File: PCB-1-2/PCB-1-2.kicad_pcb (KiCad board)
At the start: 2 copper layers, 4 parts, among them U1 LTC1298IS8_PBF, U2 LTC1451IS8-PBF, U3 HI-3110PSIF, U4 FT231XS-R

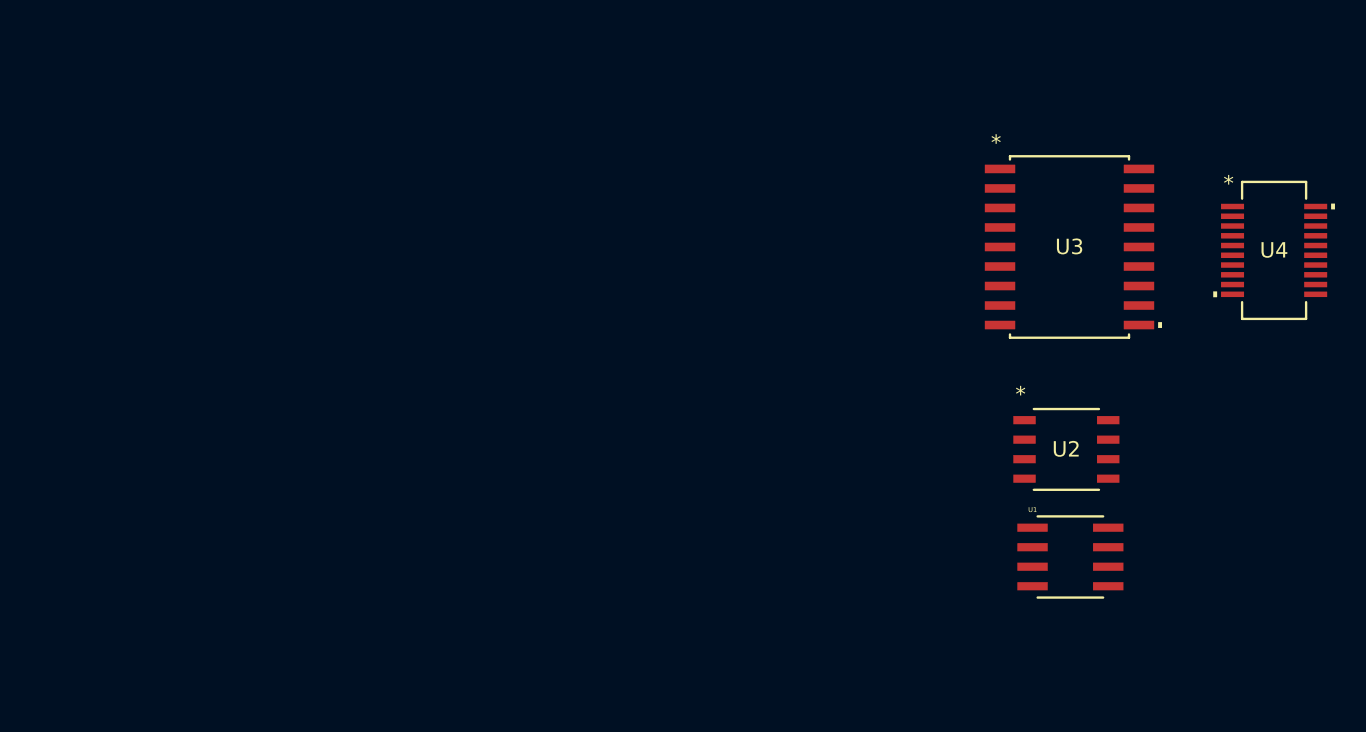
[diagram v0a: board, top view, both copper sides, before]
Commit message: Added misc components and added complimentary parts for the MCU
- Added the ADP7104 5v & 3.3V LDO's
- Added the Watchdog and connected it
- Added complimentary components for STM32
- Figured out the desired crystal and complimentary components
- Added Debug port for the ST-Link v3-MINIE
- Assigned footprints for all capacitors and most resistors
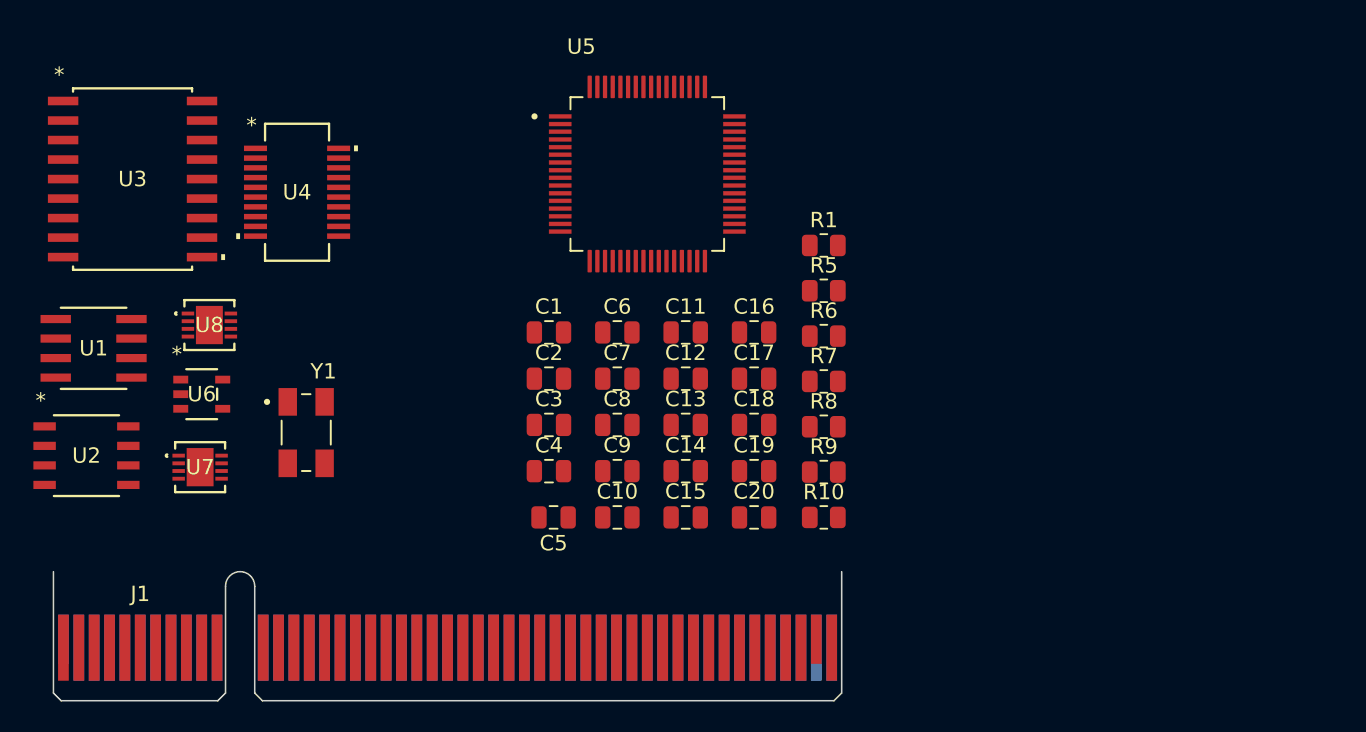
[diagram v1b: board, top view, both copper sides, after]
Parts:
- added C1: 4.7uF, Capacitor_SMD:C_0805_2012Metric, F.Cu at (61.6, 43.0)
- added C10: 100nF, Capacitor_SMD:C_0805_2012Metric, F.Cu at (66.0, 55.0)
- added C11: 100nF, Capacitor_SMD:C_0805_2012Metric, F.Cu at (70.5, 43.0)
- added C12: 10uF, Capacitor_SMD:C_0805_2012Metric, F.Cu at (70.5, 46.0)
- added C13: 10nF, Capacitor_SMD:C_0805_2012Metric, F.Cu at (70.5, 49.0)
- added C14: 1uF, Capacitor_SMD:C_0805_2012Metric, F.Cu at (70.5, 52.0)
- added C15: 1uF, Capacitor_SMD:C_0805_2012Metric, F.Cu at (70.5, 55.0)
- added C16: 10pF, Capacitor_SMD:C_0805_2012Metric, F.Cu at (75.0, 43.0)
- added C17: 10pF, Capacitor_SMD:C_0805_2012Metric, F.Cu at (75.0, 46.0)
- added C18: 2.2uF, Capacitor_SMD:C_0805_2012Metric, F.Cu at (75.0, 49.0)
- added C19: 2.2uF, Capacitor_SMD:C_0805_2012Metric, F.Cu at (75.0, 52.0)
- added C2: .1uF, Capacitor_SMD:C_0805_2012Metric, F.Cu at (61.6, 46.0)
- added C20: .1uF, Capacitor_SMD:C_0805_2012Metric, F.Cu at (75.0, 55.0)
- added C3: 47pF, Capacitor_SMD:C_0805_2012Metric, F.Cu at (61.6, 49.0)
- added C4: 47pF, Capacitor_SMD:C_0805_2012Metric, F.Cu at (61.6, 52.0)
- added C5: 100nF, Capacitor_SMD:C_0805_2012Metric, F.Cu at (61.9, 55.0)
- added C6: 10nF, Capacitor_SMD:C_0805_2012Metric, F.Cu at (66.0, 43.0)
- added C7: 100nF, Capacitor_SMD:C_0805_2012Metric, F.Cu at (66.0, 46.0)
- added C8: 100nF, Capacitor_SMD:C_0805_2012Metric, F.Cu at (66.0, 49.0)
- added C9: 100nF, Capacitor_SMD:C_0805_2012Metric, F.Cu at (66.0, 52.0)
- added J1: Bus_PCI_Express_x8, Connector_PCBEdge:BUS_PCIexpress_x8, F.Cu at (30.0, 63.5)
- added R1: 5.1K, Resistor_SMD:R_0805_2012Metric, F.Cu at (79.5, 37.3)
- added R10: 100k, Resistor_SMD:R_0805_2012Metric, F.Cu at (79.5, 55.0)
- added R5: 100k, Resistor_SMD:R_0805_2012Metric, F.Cu at (79.5, 40.3)
- added R6: 17.4k, Resistor_SMD:R_0805_2012Metric, F.Cu at (79.5, 43.2)
- added R7: 5.6k, Resistor_SMD:R_0805_2012Metric, F.Cu at (79.5, 46.2)
- added R8: 17.4k, Resistor_SMD:R_0805_2012Metric, F.Cu at (79.5, 49.1)
- added R9: 10k, Resistor_SMD:R_0805_2012Metric, F.Cu at (79.5, 52.1)
- added U5: STM32F103RBT6, SDII LIB:QFP50P1200X1200X160-64N, F.Cu at (68.0, 32.7)
- added U6: STWD100YNXWY3F, SDII LIB:SOT23-5_STM, F.Cu at (39.0, 47.0)
- added U7: ADP7104ACPZ-5V, SDII LIB:CP_8_5_ADI, F.Cu at (38.9, 51.8)
- added U8: ADP7104ACPZ-3.3V, SDII LIB:CP_8_5_ADI, F.Cu at (39.5, 42.5)
- added Y1: 8MHz Crystal, SDII LIB:XTAL_ABM3B-8.000MHZ-10-1-U-T, F.Cu at (45.8, 49.5)
- moved U1 65.0 mm to (32.0, 44.0)
- moved U2 63.8 mm to (31.5, 51.0)
- moved U4 63.7 mm to (45.2, 33.9)
- moved U3 61.1 mm to (34.5, 33.0)
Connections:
- U1 pad 1: unconnected-(U1-*CS/SHDN-Pad1) -> SPI2_CS
- U1 pad 2: unconnected-(U1-CH0-Pad2) -> ADC_CH0
- U1 pad 3: unconnected-(U1-CH1-Pad3) -> ADC_CH1
- U1 pad 4: unconnected-(U1-GND-Pad4) -> +5V
- U1 pad 5: unconnected-(U1-DIN-Pad5) -> SPI2_MOSI
- U1 pad 6: unconnected-(U1-DOUT-Pad6) -> SPI2_MISO
- U1 pad 7: unconnected-(U1-CLK-Pad7) -> SPI2_CLK
- U1 pad 8: unconnected-(U1-VCC(VREF)-Pad8) -> +5V
- U2 pad 1: unconnected-(U2-CLK-Pad1) -> SPI2_CLK
- U2 pad 2: unconnected-(U2-DIN-Pad2) -> SPI2_MOSI
- U2 pad 3: unconnected-(U2-*CS/LD-Pad3) -> SPI2_CS
- U2 pad 4: unconnected-(U2-DOUT-Pad4) -> SPI2_MISO
- U2 pad 5: unconnected-(U2-GND-Pad5) -> +5V
- U2 pad 6: unconnected-(U2-REF-Pad6) -> Net-(U2-REF)
- U2 pad 7: unconnected-(U2-VOUT-Pad7) -> DAC_OUT
- U2 pad 8: unconnected-(U2-VCC-Pad8) -> Net-(U2-REF)
- U4 pad 11: unconnected-(U4-USBDP-Pad11) -> Net-(U4-USBDP)
- U4 pad 12: unconnected-(U4-USBDM-Pad12) -> Net-(U4-USBDM)
- U4 pad 13: unconnected-(U4-3V3OUT-Pad13) -> FT231_3V3OUT
- U4 pad 14: unconnected-(U4-RESET#-Pad14) -> FT231_3V3OUT
- U4 pad 15: unconnected-(U4-VCC-Pad15) -> Net-(U4-VCC)
- U4 pad 16: unconnected-(U4-GND-Pad16) -> Net-(C5-Pad2)
- U4 pad 3: unconnected-(U4-VCCIO-Pad3) -> FT231_3V3OUT
- U4 pad 6: unconnected-(U4-GND-Pad6) -> Net-(C5-Pad2)
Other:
- board outline added: 51.3 x 8.4 mm

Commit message: Updated a few things
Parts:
- moved U4 26.7 mm to (71.3, 28.2)
- moved U8 18.0 mm to (52.5, 55.0)
- moved U5 11.2 mm to (57.2, 35.7)
- moved Y1 9.67 mm to (44.0, 40.0)
- moved U7 8.73 mm to (47.0, 55.0)
- moved C5 7.50 mm to (69.4, 55.0)
- moved C10 7.50 mm to (73.5, 55.0)
- moved C11 7.50 mm to (78.0, 43.0)
- moved C12 7.50 mm to (78.0, 46.0)
- moved C13 7.50 mm to (78.0, 49.0)
- moved C14 7.50 mm to (78.0, 52.0)
- moved C15 7.50 mm to (78.0, 55.0)
- moved C16 7.50 mm to (82.5, 43.0)
- moved C17 7.50 mm to (82.5, 46.0)
- moved C18 7.50 mm to (82.5, 49.0)
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
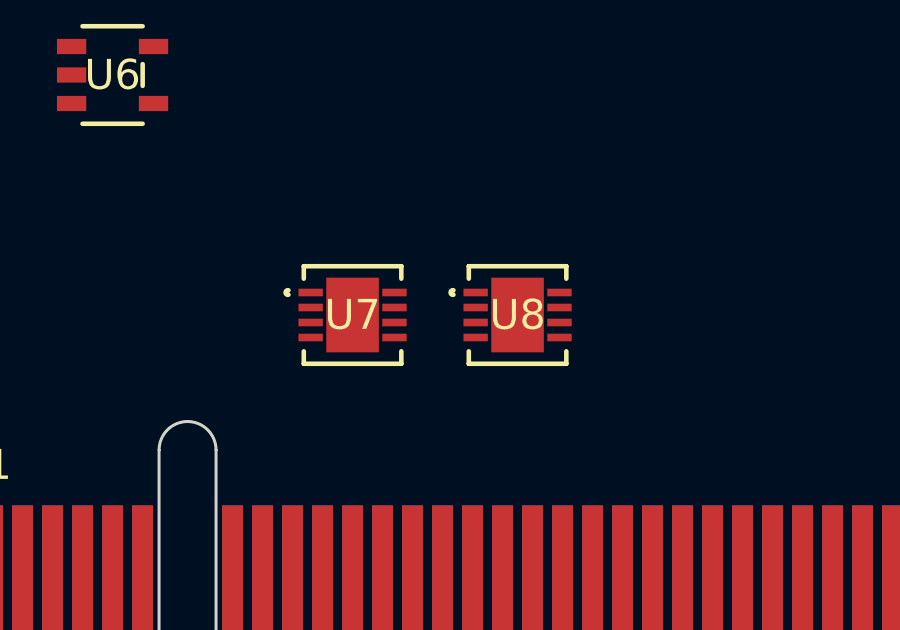
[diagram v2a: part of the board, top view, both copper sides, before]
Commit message: Finished adding connections to the FTDI chip
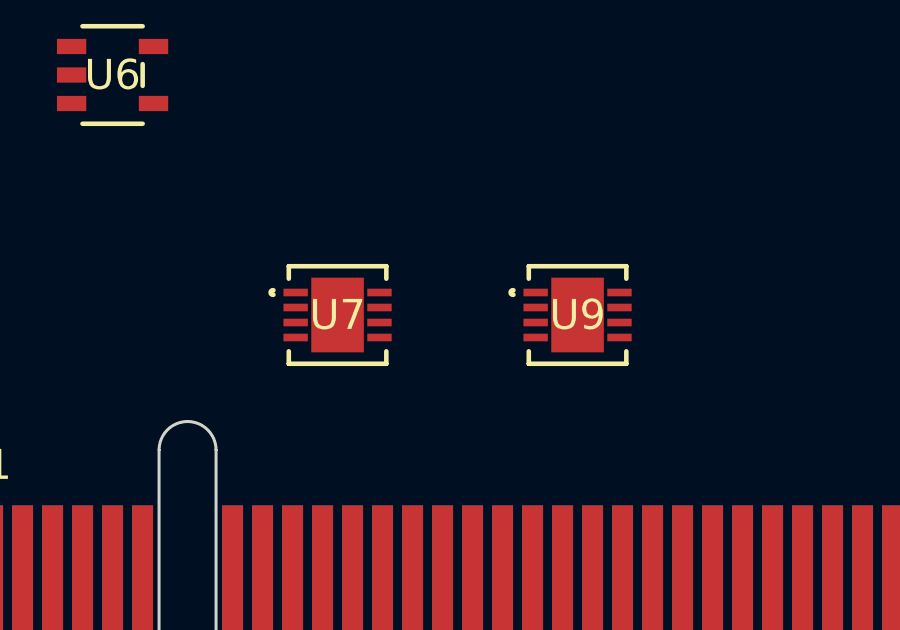
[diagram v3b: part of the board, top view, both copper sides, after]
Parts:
- removed U8: ADP7104ACPZ-3.3V, SDII LIB:CP_8_5_ADI
- added U9: ADP7104ACPZ-R7 (5v), SDII LIB:CP_8_5_ADI, F.Cu at (54.5, 55.0)
- C12: value 10uF -> 4.7uF
- U7: value ADP7104ACPZ-5V -> ADP7104ACPZ-R7 (v3.3)
- moved U7 0.50 mm to (46.5, 55.0)
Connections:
- net Net-(U5-PD0_OSC_IN) renamed /OSC_IN
- net Net-(U5-PD1_OSC_OUT) renamed /OSC_OUT
- C1 pad 1: +5V -> V+_FROM_PCIE
- C1 pad 2: +5V -> V+_FROM_PCIE
- C10 pad 1: +5V -> V+_FROM_PCIE
- C11 pad 1: +5V -> V+_FROM_PCIE
- C12 pad 1: +5V -> V+_FROM_PCIE
- C13 pad 1: +3.3VA -> +3.3V
- C13 pad 2: +5V -> V+_FROM_PCIE
- C14 pad 1: +3.3VA -> +3.3V
- C14 pad 2: +5V -> V+_FROM_PCIE
- C15 pad 1: +3.3VA -> +3.3V
- C15 pad 2: +5V -> V+_FROM_PCIE
- C16 pad 2: +5V -> V+_FROM_PCIE
- C17 pad 2: +5V -> V+_FROM_PCIE
- C18 pad 1: +5V -> V+_FROM_PCIE
- C18 pad 2: +5V -> V+_FROM_PCIE
- C19 pad 2: +5V -> V+_FROM_PCIE
- C2 pad 2: +5V -> V+_FROM_PCIE
- C20 pad 2: +5V -> V+_FROM_PCIE
- C3 pad 2: +5V -> V+_FROM_PCIE
- C4 pad 2: +5V -> V+_FROM_PCIE
- C7 pad 1: +5V -> V+_FROM_PCIE
- C8 pad 1: +5V -> V+_FROM_PCIE
- C9 pad 1: +5V -> V+_FROM_PCIE
- R1 pad 2: +5V -> V+_FROM_PCIE
- R10 pad 2: Net-(U8-PG) -> Net-(U7-PG)
- R5 pad 1: +5V -> V+_FROM_PCIE
- R5 pad 2: Net-(U7-PG) -> Net-(U9-PG)
- R6 pad 1: Net-(U7-SENSE/ADJ) -> Net-(U9-SENSE/ADJ)
- R6 pad 2: +5V -> V+_FROM_PCIE
- R7 pad 1: +5V -> V+_FROM_PCIE
- R7 pad 2: Net-(U7-SENSE/ADJ) -> Net-(U9-SENSE/ADJ)
- R8 pad 1: Net-(U8-SENSE/ADJ) -> Net-(U7-SENSE/ADJ)
- R9 pad 1: +5V -> V+_FROM_PCIE
- R9 pad 2: Net-(U8-SENSE/ADJ) -> Net-(U7-SENSE/ADJ)
- U1 pad 4: +5V -> V+_FROM_PCIE
- U1 pad 8: +5V -> V+_FROM_PCIE
- U2 pad 5: +5V -> V+_FROM_PCIE
- U5 pad 12: +5V -> V+_FROM_PCIE
- U5 pad 13: +3.3VA -> +3.3V
- U5 pad 18: +5V -> V+_FROM_PCIE
- U5 pad 31: +5V -> V+_FROM_PCIE
- U5 pad 33: unconnected-(U5-PB12-Pad33) -> SPI2_NSS
- U5 pad 47: +5V -> V+_FROM_PCIE
- U5 pad 60: +5V -> V+_FROM_PCIE
- U5 pad 63: +5V -> V+_FROM_PCIE
- U6 pad 2: +5V -> V+_FROM_PCIE
- U7 pad 1: +5V -> +3.3V
- U7 pad 3: +5V -> V+_FROM_PCIE
- U7 pad 6: +5V -> V+_FROM_PCIE
- U7 pad 9: +5V -> V+_FROM_PCIE
- Y1 pad 2: +5V -> V+_FROM_PCIE
- Y1 pad 4: +5V -> V+_FROM_PCIE

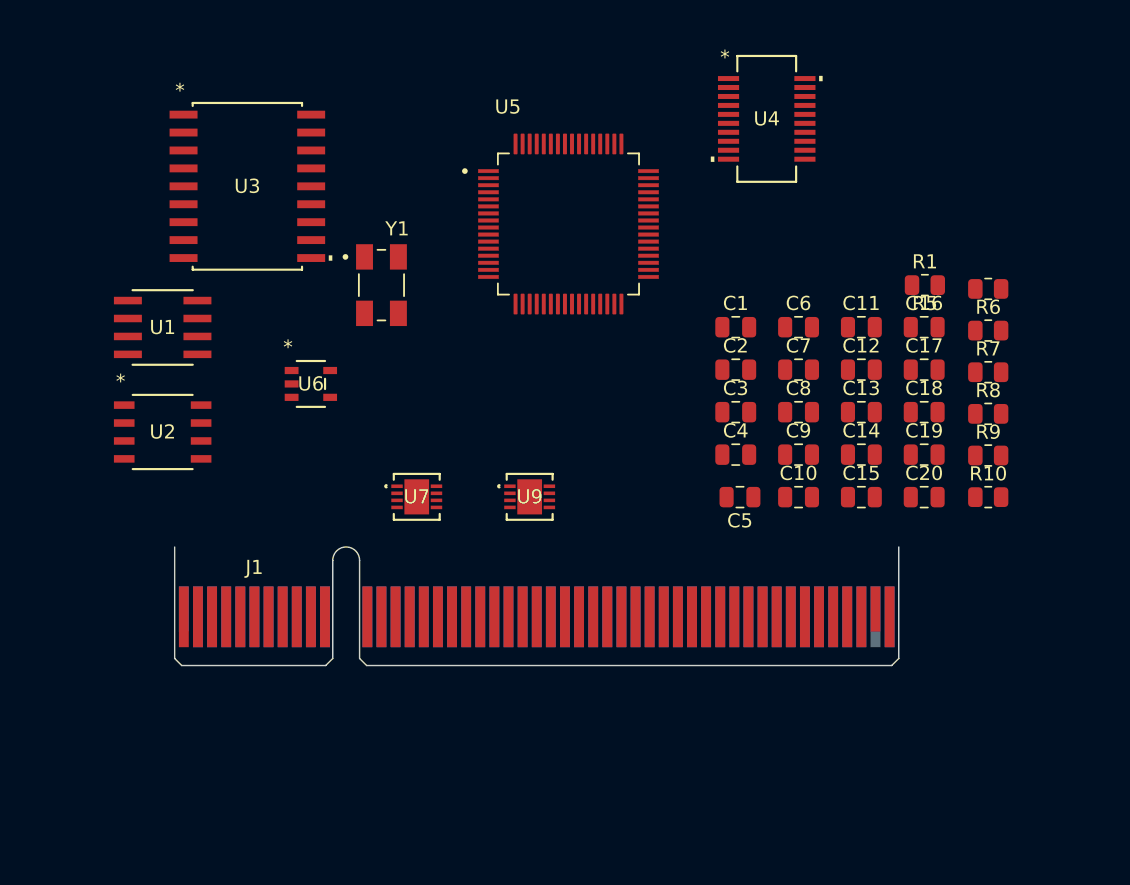
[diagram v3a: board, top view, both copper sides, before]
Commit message: Updated schematic to add the RTD and Transducer signal conditioning
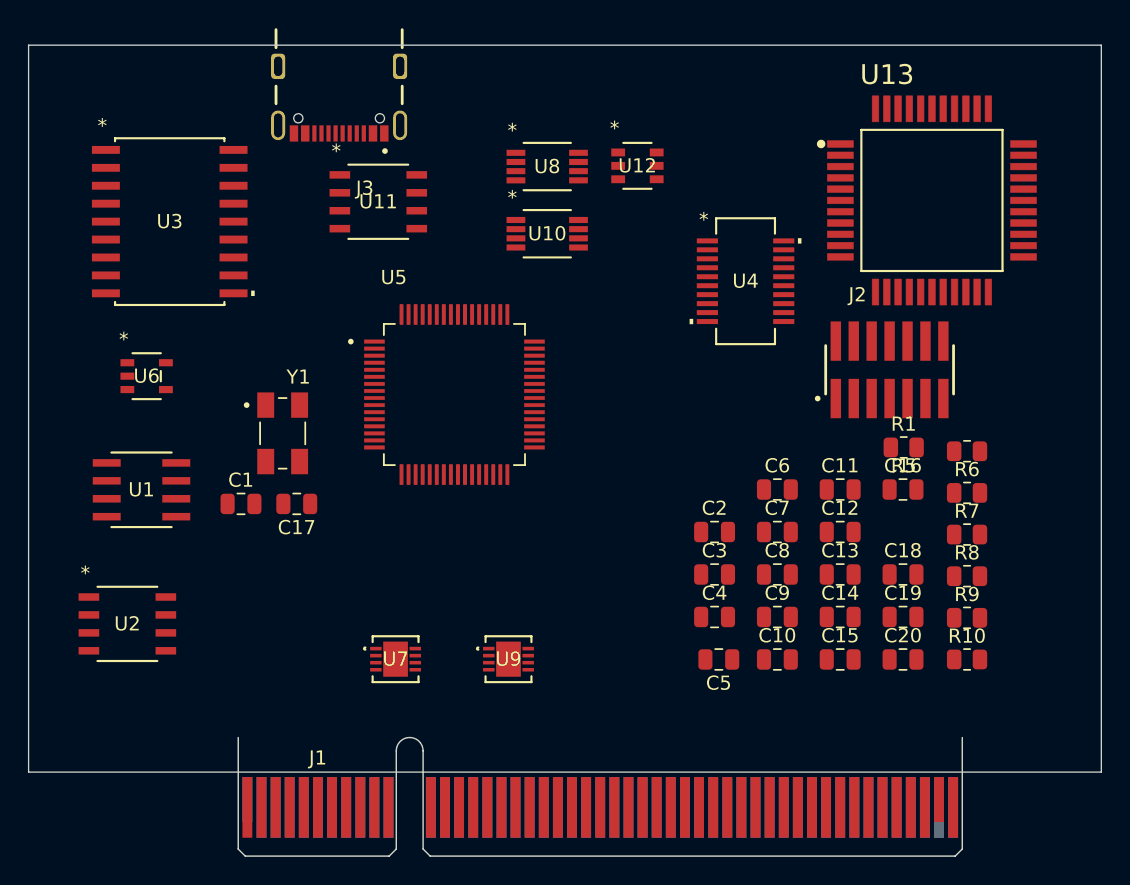
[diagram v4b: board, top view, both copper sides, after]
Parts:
- added J2: ST STDC14 (Debug Connector), SDII LIB:SAMTEC_FTSH-107-01-F-DV-K-P-TR, F.Cu at (80.0, 46.0)
- added J3: USB4105-GF-A, SDII LIB:GCT_USB4105-GF-A, F.Cu at (41.0, 24.5)
- added U10: INA827AIDGKR, SDII LIB:DGK8_TEX, F.Cu at (55.7, 36.4)
- added U11: LTC1250CS8-PBF, SDII LIB:SO-8_S_LIT, F.Cu at (43.8, 34.1)
- added U12: REF3425MDBVTEP, SDII LIB:SOT-23-6_TEX, F.Cu at (62.1, 31.5)
- added U13: HI-3585APQI, SDII LIB:QFP80P1390X1390X150-44N, F.Cu at (83.0, 34.0)
- added U8: OPA2187IDGKR, SDII LIB:DGK8_TEX, F.Cu at (55.7, 31.6)
- C18, C19: value 2.2uF -> 4.7uF
- moved C17 45.5 mm to (38.0, 55.5), turned to 180 degrees
- moved C1 37.2 mm to (34.0, 55.5)
- moved U5 14.5 mm to (49.2, 47.8)
- moved J1 14.2 mm to (34.5, 77.0)
- moved U2 13.8 mm to (26.0, 64.0)
- moved Y1 12.6 mm to (37.0, 50.5)
- moved U6 11.6 mm to (27.4, 46.5)
- moved C11 11.6 mm to (76.5, 54.5)
- moved C12 11.6 mm to (76.5, 57.5)
- moved C13 11.6 mm to (76.5, 60.5)
- moved C14 11.6 mm to (76.5, 63.5)
- moved C16 11.6 mm to (81.0, 54.5)
- moved C18 11.6 mm to (81.0, 60.5)
- moved C19 11.6 mm to (81.0, 63.5)
- moved C2 11.6 mm to (67.6, 57.5)
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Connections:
- net USB_V+ renamed USB_VDD
- C1 pad 1: V+_FROM_PCIE -> +5V
- C1 pad 2: V+_FROM_PCIE -> Transducer-
- C10 pad 1: V+_FROM_PCIE -> Transducer-
- C11 pad 1: V+_FROM_PCIE -> Transducer-
- C12 pad 1: V+_FROM_PCIE -> Transducer-
- C13 pad 2: V+_FROM_PCIE -> Transducer-
- C14 pad 2: V+_FROM_PCIE -> Transducer-
- C15 pad 2: V+_FROM_PCIE -> Transducer-
- C16 pad 2: V+_FROM_PCIE -> Transducer-
- C17 pad 2: V+_FROM_PCIE -> Transducer-
- C18 pad 1: V+_FROM_PCIE -> +5V
- C18 pad 2: V+_FROM_PCIE -> Transducer-
- C19 pad 2: V+_FROM_PCIE -> Transducer-
- C2 pad 1: Net-(U2-REF) -> Net-(U2-VCC)
- C2 pad 2: V+_FROM_PCIE -> Transducer-
- C20 pad 2: V+_FROM_PCIE -> Transducer-
- C3 pad 2: V+_FROM_PCIE -> Transducer-
- C4 pad 2: V+_FROM_PCIE -> Transducer-
- C5 pad 2: Net-(C5-Pad2) -> Transducer-
- C6 pad 1: Net-(C5-Pad2) -> Transducer-
- C7 pad 1: V+_FROM_PCIE -> Transducer-
- C8 pad 1: V+_FROM_PCIE -> Transducer-
- C9 pad 1: V+_FROM_PCIE -> Transducer-
- R1 pad 2: V+_FROM_PCIE -> Transducer-
- R5 pad 1: V+_FROM_PCIE -> +5V
- R6 pad 2: V+_FROM_PCIE -> +5V
- R7 pad 1: V+_FROM_PCIE -> Transducer-
- R9 pad 1: V+_FROM_PCIE -> Transducer-
- U1 pad 4: V+_FROM_PCIE -> Transducer-
- U1 pad 8: V+_FROM_PCIE -> +5V
- U2 pad 5: V+_FROM_PCIE -> Transducer-
- U2 pad 6: Net-(U2-REF) -> unconnected-(U2-REF-Pad6)
- U2 pad 8: Net-(U2-REF) -> Net-(U2-VCC)
- U3 pad 1: unconnected-(U3-VLOGIC-Pad1) -> +3.3V
- U3 pad 11: unconnected-(U3-VDD-Pad11) -> +5V
- U3 pad 4: unconnected-(U3-GP1-Pad4) -> Net-(D1-A)
- U3 pad 5: unconnected-(U3-GP2-Pad5) -> Net-(D2-A)
- U3 pad 8: unconnected-(U3-GND-Pad8) -> Transducer-
- U4 pad 10: unconnected-(U4-CBUS2-Pad10) -> /USART_RXLED
- U4 pad 16: Net-(C5-Pad2) -> Transducer-
- U4 pad 17: unconnected-(U4-CBUS1-Pad17) -> Net-(D4-K)
- U4 pad 20: unconnected-(U4-TXD-Pad20) -> USART2_RX
- U4 pad 4: unconnected-(U4-RXD-Pad4) -> USART2_TX
- U4 pad 6: Net-(C5-Pad2) -> Transducer-
- U5 pad 12: V+_FROM_PCIE -> Transducer-
- U5 pad 18: V+_FROM_PCIE -> Transducer-
- U5 pad 31: V+_FROM_PCIE -> Transducer-
- U5 pad 47: V+_FROM_PCIE -> Transducer-
- U5 pad 55: SWO -> unconnected-(U5-PB3-Pad55)
- U5 pad 60: V+_FROM_PCIE -> Transducer-
- U5 pad 63: V+_FROM_PCIE -> Transducer-
- U6 pad 2: V+_FROM_PCIE -> Transducer-
- U7 pad 3: V+_FROM_PCIE -> Transducer-
- U7 pad 6: V+_FROM_PCIE -> Transducer-
- U7 pad 9: V+_FROM_PCIE -> Transducer-
- U9 pad 1: V+_FROM_PCIE -> +5V
- U9 pad 3: V+_FROM_PCIE -> Transducer-
- U9 pad 6: V+_FROM_PCIE -> Transducer-
- U9 pad 9: V+_FROM_PCIE -> Transducer-
- Y1 pad 2: V+_FROM_PCIE -> Transducer-
- Y1 pad 4: V+_FROM_PCIE -> Transducer-
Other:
- board size 51.3 x 8.4 mm -> 76 x 51.5 mm
